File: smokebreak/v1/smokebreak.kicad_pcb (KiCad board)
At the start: 6 copper layers, 94 x 52 mm, 204 parts, among them J1 XT60 male, J10 JST-XH 4S, J11 JST-XH 3S, J12 JST-XH 2S, J2 XT30 male, J3 XT60 female, J4 XT30 female, J5 JST-XH 6S, J6 SWD, J7 TFT1901 FPC, J8 USB-C, J9 JST-XH 5S, Q1 input FET, Q10 BC817, Q11 BSC070N10LS5, Q2 output FET, Q3 SUD50P10-43L, Q4 MMBTA42, Q5 BC817, Q6 MMBT5401, Q7 MMBT5401, Q8 2N7002, Q9 AO3400A, SW1 ON-OFF-(ON), SW2 Limit -, SW3 Limit +, U1 TPS48000, U10 SN74AHCT1G125, U11 USBLC6-2SC6, U12 LMV331, U2 INA181A2, U3 LMR36506R5, U4 TLV75533, U5 STM32G0B1RBT6, U6 DRV5032FA, U7 74LVC1G11, U8 LMV331, U9 SN74LVC1G74

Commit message: smokebreak v1: polished board (2 DRC errors, 2 open), polish keeps power nets' own copper
Co-Authored-By: Claude Opus 5.5 <noreply@anthropic.com>
Claude-Session: https://claude.ai/code/session_01SBnFJLvm1wBa1jZy4RXnma
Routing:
- net PRE_ON: track 41.2 -> 36.8 mm
- net USB_DP_C: track 17.9 -> 15.9 mm
- net DRONE_NEG: track 6.36 -> 4.91 mm
- net MCU_EN: track 28.9 -> 27.8 mm
- net BAL5: track 67.8 -> 66.8 mm
- net BAL7_ADC: track 21.9 -> 21.0 mm
- net VIN_SENSE: track 33.0 -> 32.5 mm
- net SNS_GND: track 24.5 -> 24.7 mm, vias 2 -> 3

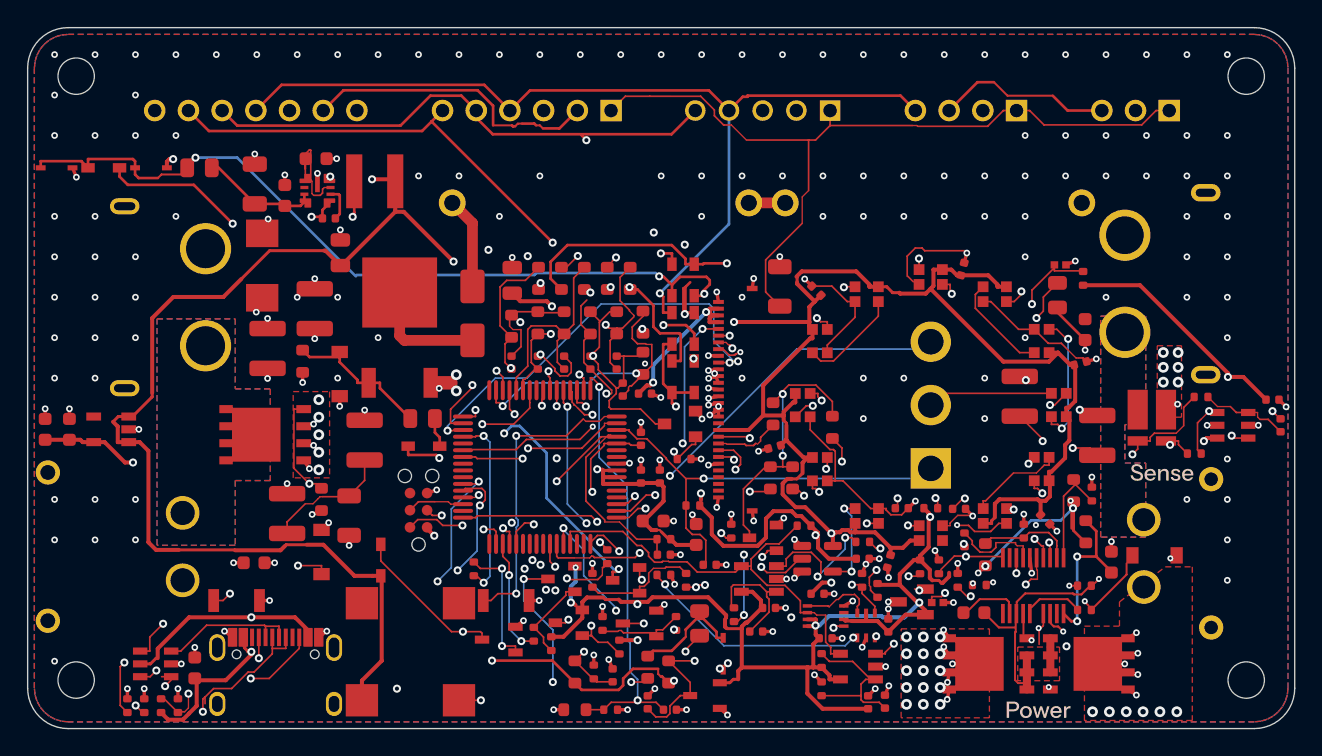
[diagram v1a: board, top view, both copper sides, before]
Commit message: smokebreak v1: final board with 2S-6S balance sockets: DRC 0/0/0, netlist matches, PCBWay files, STEP, renders
Five keyed JST-XH sockets on the back wall, USB-C on the front wall, series
2 x 3.9 Ohm pre-charge. KiCad 10 DRC: 0 errors, 0 warnings, 0 unconnected.
3S socket uses KiCad's stock JST model (the vendor model was rotated).

Co-Authored-By: Claude Opus 5.5 <noreply@anthropic.com>
Claude-Session: https://claude.ai/code/session_01SBnFJLvm1wBa1jZy4RXnma
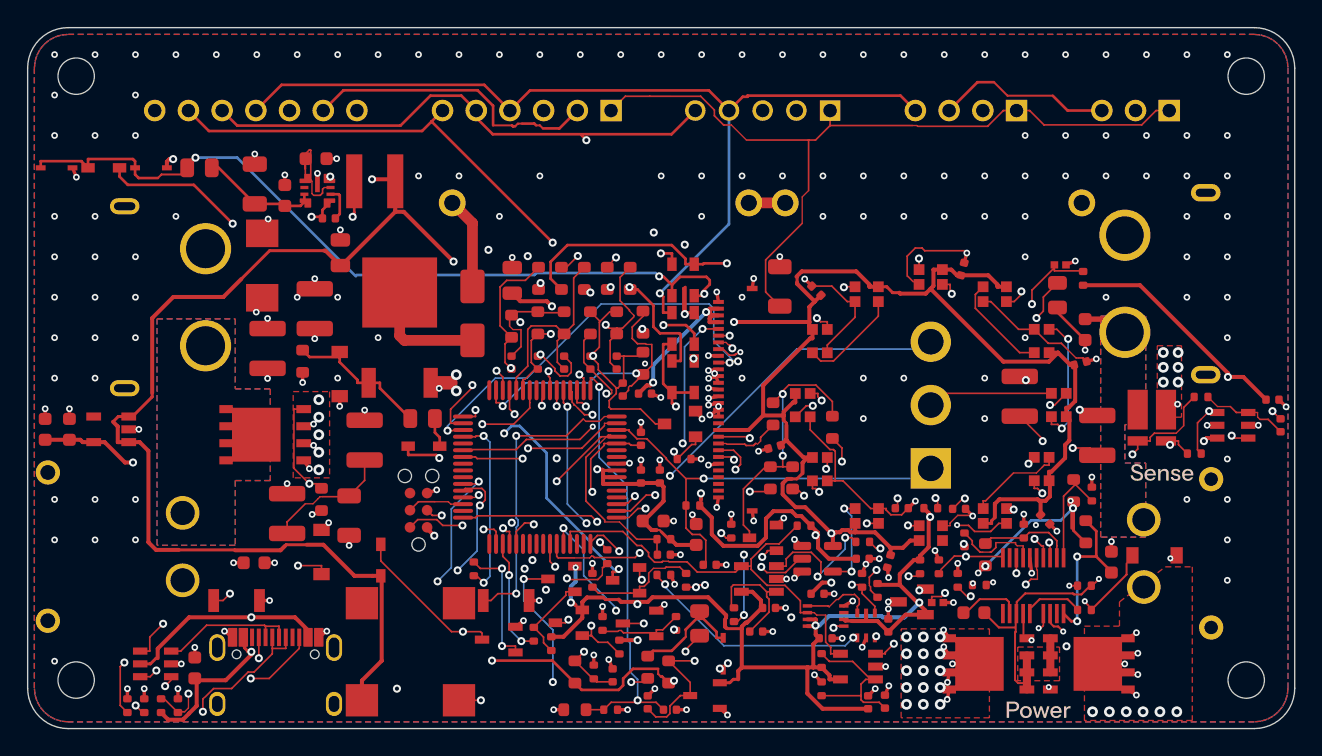
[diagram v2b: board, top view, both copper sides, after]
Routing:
- net BAL7: track 41.1 -> 72.3 mm
- net PRE_ON: track 36.8 -> 22.4 mm, vias 7 -> 5
- net ARM_CLK: track 31.3 -> 26.5 mm
- net +3V3: track 251.4 -> 247.7 mm
- net BAL5_ADC: track 33.7 -> 30.7 mm
- net DRONE_NEG: track 4.91 -> 6.36 mm
- net USB_DP_C: track 15.9 -> 14.7 mm
- net SNS_GND: track 24.7 -> 23.6 mm
- net GUARD_OPEN: track 38.1 -> 37.3 mm
- net VOUT_SENSE: track 26.5 -> 25.9 mm
- net GND: vias 234 -> 233

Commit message: Layout A placement: MCU tucked under the resistors, districts packed on rows, SWD pads to the underside
Co-Authored-By: Claude Opus 5.5 <noreply@anthropic.com>
Claude-Session: https://claude.ai/code/session_01SBnFJLvm1wBa1jZy4RXnma
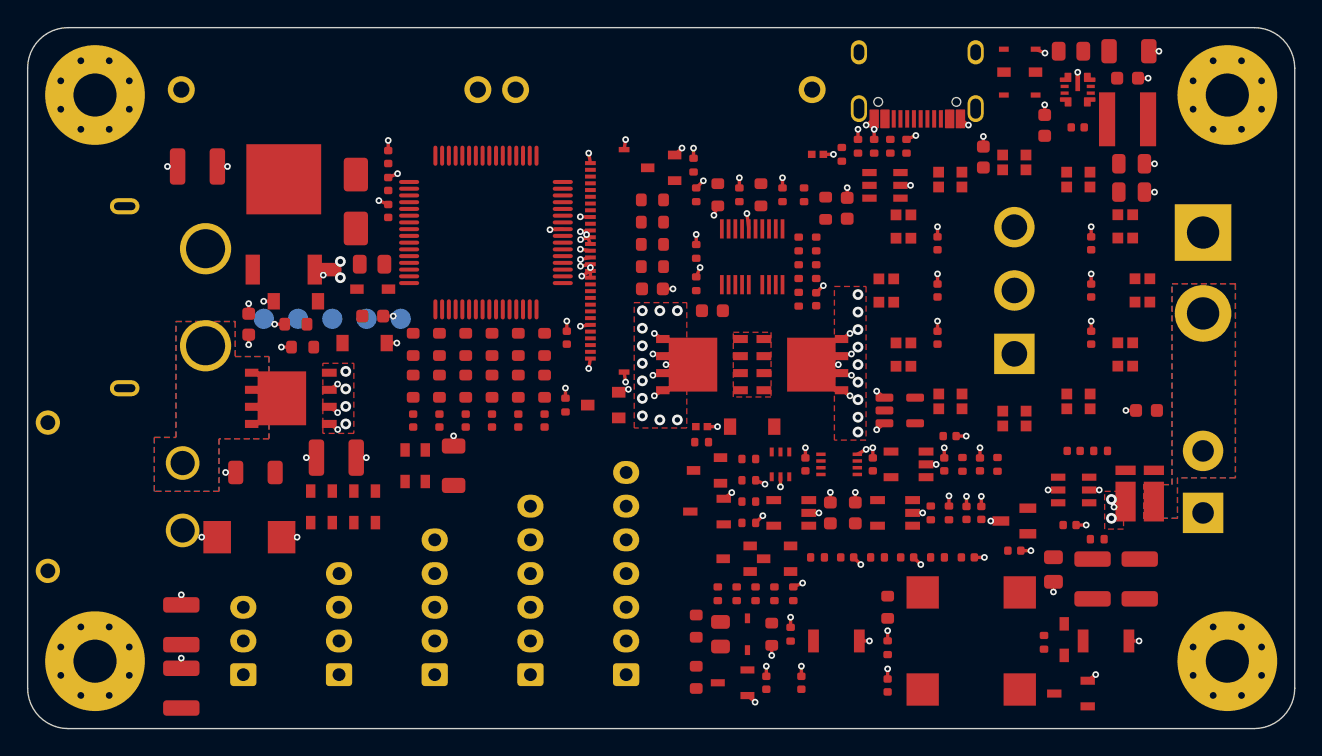
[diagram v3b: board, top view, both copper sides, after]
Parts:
- H1, H2, H3, H4: value M2.5 -> M3; footprint MountingHole_2.7mm_M2.5 -> MountingHole_M3_Washer
- J10: footprint CONN-TH_5P-P2.50_S5B-XH-A-LF-SN -> JST_XH_B5B-XH-A_1x05_P2.50mm_Vertical
- J11: footprint CONN-TH_S4B-XH-A-LF-SN -> JST_XH_B4B-XH-A_1x04_P2.50mm_Vertical
- J12: footprint CONN-TH_S3B-XH-A-LF-SN -> JST_XH_B3B-XH-A_1x03_P2.50mm_Vertical
- J3: value XT60 female -> XT60 female lead; footprint TH_2P-XT60PW-F -> WirePads_12AWG
- J4: value XT30 female -> XT30 female lead; footprint CONN-TH_XT30PW-F30.G.Y -> WirePads_16AWG
- J5: footprint CONN-TH_S7B-XH-A-LF-SN -> JST_XH_B7B-XH-A_1x07_P2.50mm_Vertical
- J6: footprint Tag-Connect_TC2030-IDC-NL_2x03_P1.27mm_Vertical -> SWD_Pads_1x5_P2.54; moved to B.Cu
- J9: footprint CONN-TH_S6B-XH-A-LF-SN -> JST_XH_B6B-XH-A_1x06_P2.50mm_Vertical
- moved J12 78.3 mm to (116.0, 148.0), turned to 90 degrees
- moved D14 72.0 mm to (173.6, 101.6)
- moved C49 69.7 mm to (170.9, 109.6)
- moved D15 68.3 mm to (173.6, 103.3)
- moved R62 68.3 mm to (161.6, 108.8)
- moved R63 68.2 mm to (162.8, 108.8)
- moved R64 68.2 mm to (164.0, 108.8)
- moved R65 68.1 mm to (165.2, 108.8)
- moved C26 65.6 mm to (181.7, 101.8), turned to 0 degrees
- moved R53 65.2 mm to (177.4, 101.8)
- moved U11 64.7 mm to (163.6, 111.7)
- moved D16 64.7 mm to (173.6, 105.0)
- moved J8 64.4 mm to (166.0, 104.3), turned to 180 degrees
- moved C27 63.1 mm to (181.6, 103.8), turned to 0 degrees
- moved J11 62.6 mm to (123.1, 148.0), turned to 90 degrees
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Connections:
- J3 pad 1: (no net) -> VOUT
- J3 pad 2: (no net) -> DRONE_NEG
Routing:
- net +3V3: track 247.7 -> 0.00 mm, vias 17 -> 0
- net +5V: track 216.7 -> 0.00 mm, vias 7 -> 0
- net VOUT: track 117.8 -> 7.25 mm, vias 18 -> 17
- net BAL3: track 94.4 -> 0.00 mm, vias 1 -> 0
- net BAL2: track 91.2 -> 0.00 mm, vias 2 -> 0
- net AUX: track 90.7 -> 0.00 mm, vias 5 -> 0
- net BAL1: track 80.2 -> 0.00 mm
- net BAL4: track 75.6 -> 0.00 mm, vias 2 -> 0
- net BAL7: track 72.3 -> 0.00 mm, vias 4 -> 0
- net VBUS: track 67.4 -> 0.00 mm, vias 3 -> 0
- net BAL5: track 66.3 -> 0.00 mm, vias 4 -> 0
- net GND: track 133.2 -> 79.2 mm, vias 233 -> 110
- net TOG_ON: track 49.4 -> 0.00 mm, vias 2 -> 0
- net BAL6: track 48.6 -> 0.00 mm, vias 2 -> 0
- net VBUS_SENSE: track 46.9 -> 0.00 mm, vias 3 -> 0
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- removed copper zone on B.Cu, net GND
- removed copper zone on In2.Cu, net GND
- removed copper zone on In3.Cu, net GND

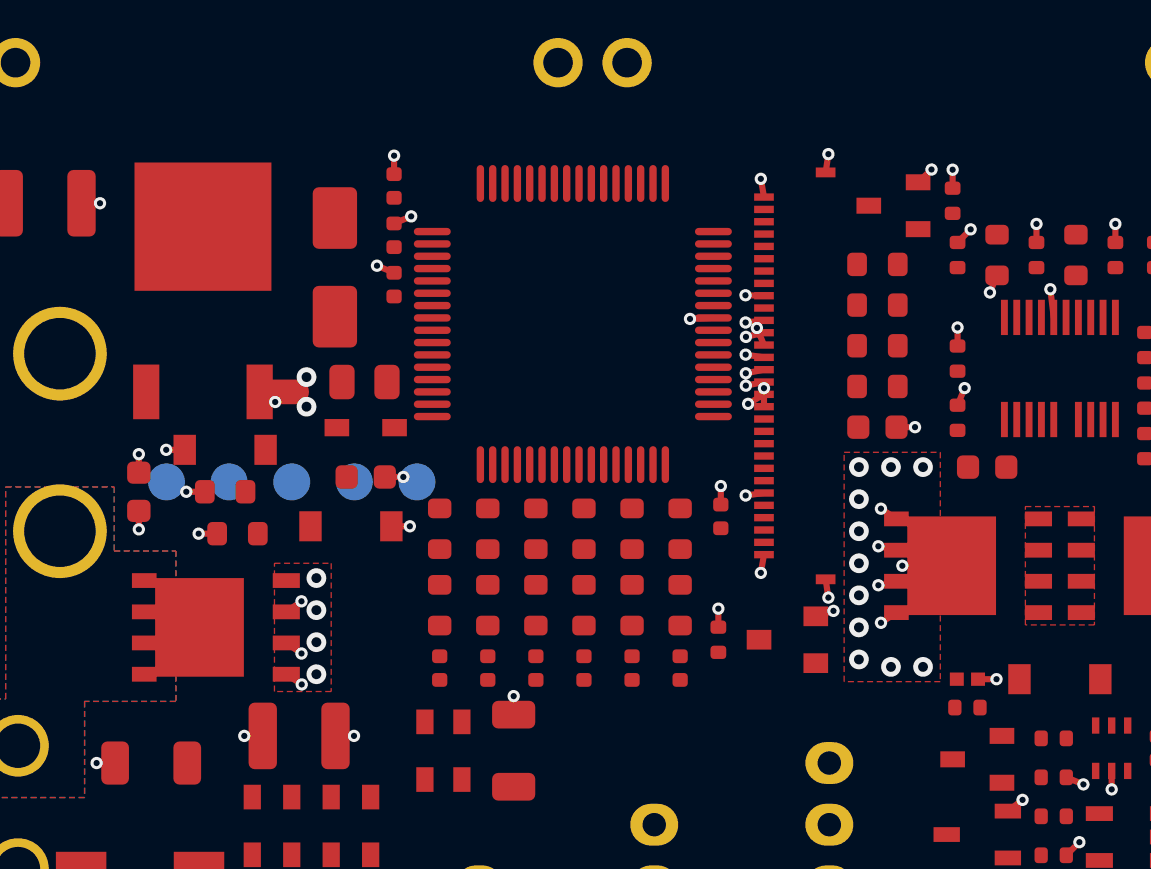
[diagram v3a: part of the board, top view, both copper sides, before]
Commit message: Layout A: Q1 drain vias in rows clear of the centre, via-free art fields, SWD pads under the MCU, routing scripts follow the new layout
Co-Authored-By: Claude Opus 5.5 <noreply@anthropic.com>
Claude-Session: https://claude.ai/code/session_01SBnFJLvm1wBa1jZy4RXnma
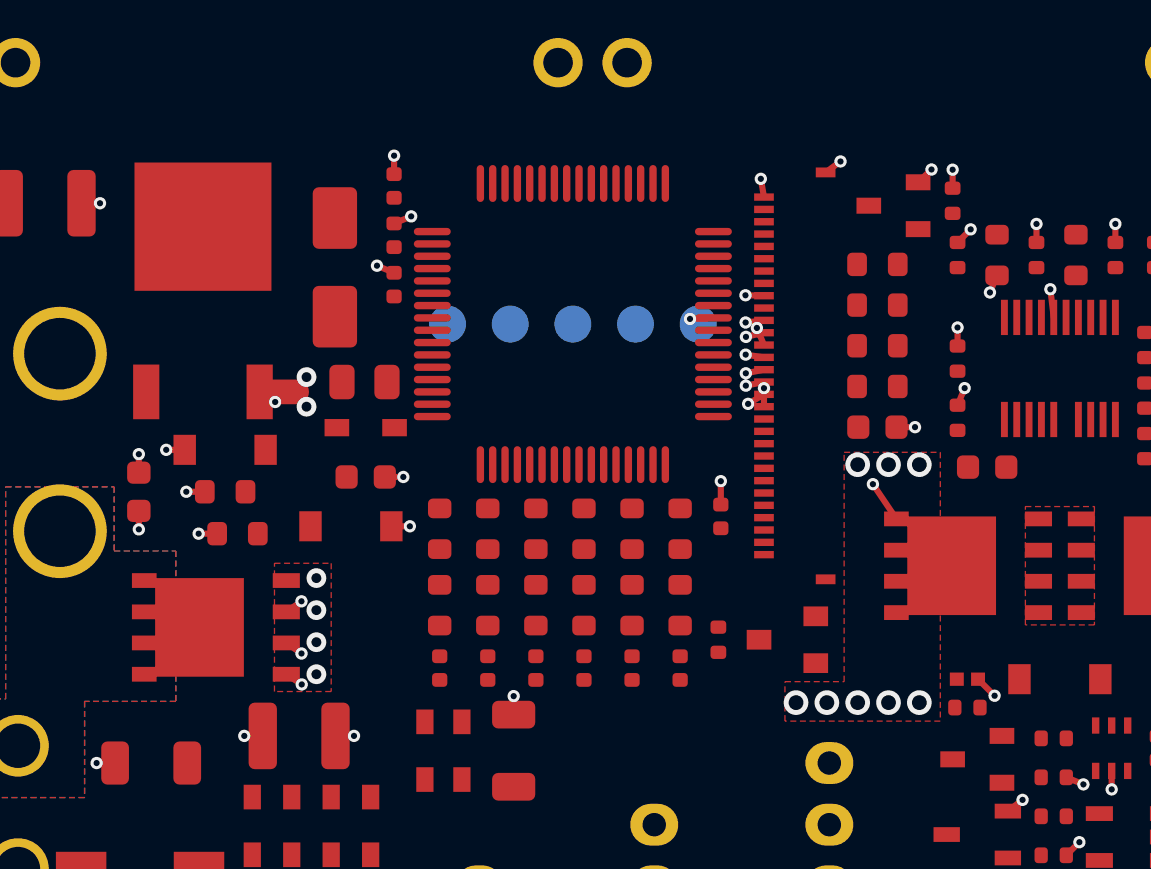
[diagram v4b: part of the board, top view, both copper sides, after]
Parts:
- moved J6 13.1 mm to (134.0, 115.2)
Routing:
- net GND: track 79.2 -> 75.9 mm, vias 110 -> 105
- net VIN: track 15.1 -> 11.8 mm, vias 29 -> 22
